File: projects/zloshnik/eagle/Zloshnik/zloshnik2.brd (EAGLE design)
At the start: 132.5 x 50.6 mm, 108 parts, among them IC1 TL5626D, IC2 78L05F, IC6 DS3234, IC7 MEGA8-AI, Q2 IRF630N, Q4 IRF630N, SW1 BUTTON-IT_1181

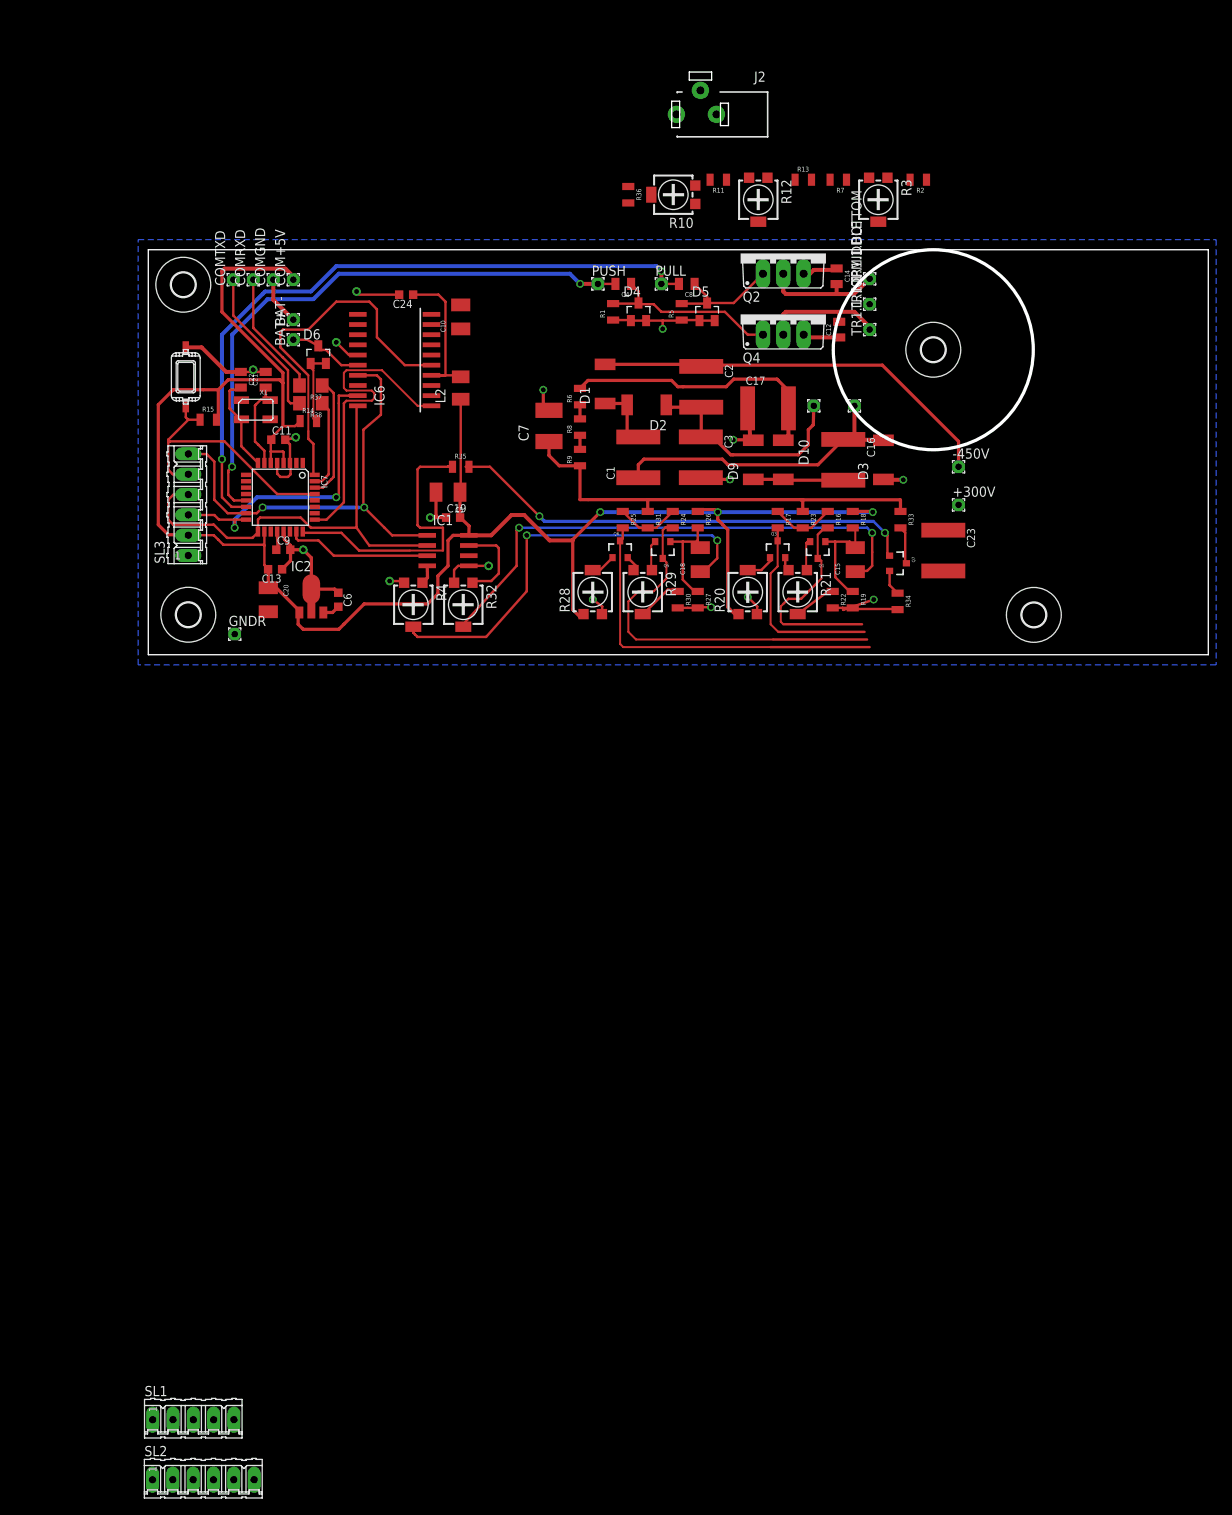
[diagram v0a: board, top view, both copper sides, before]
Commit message: +3v3 and conversion for bluetooth, more sparse layout in hv area
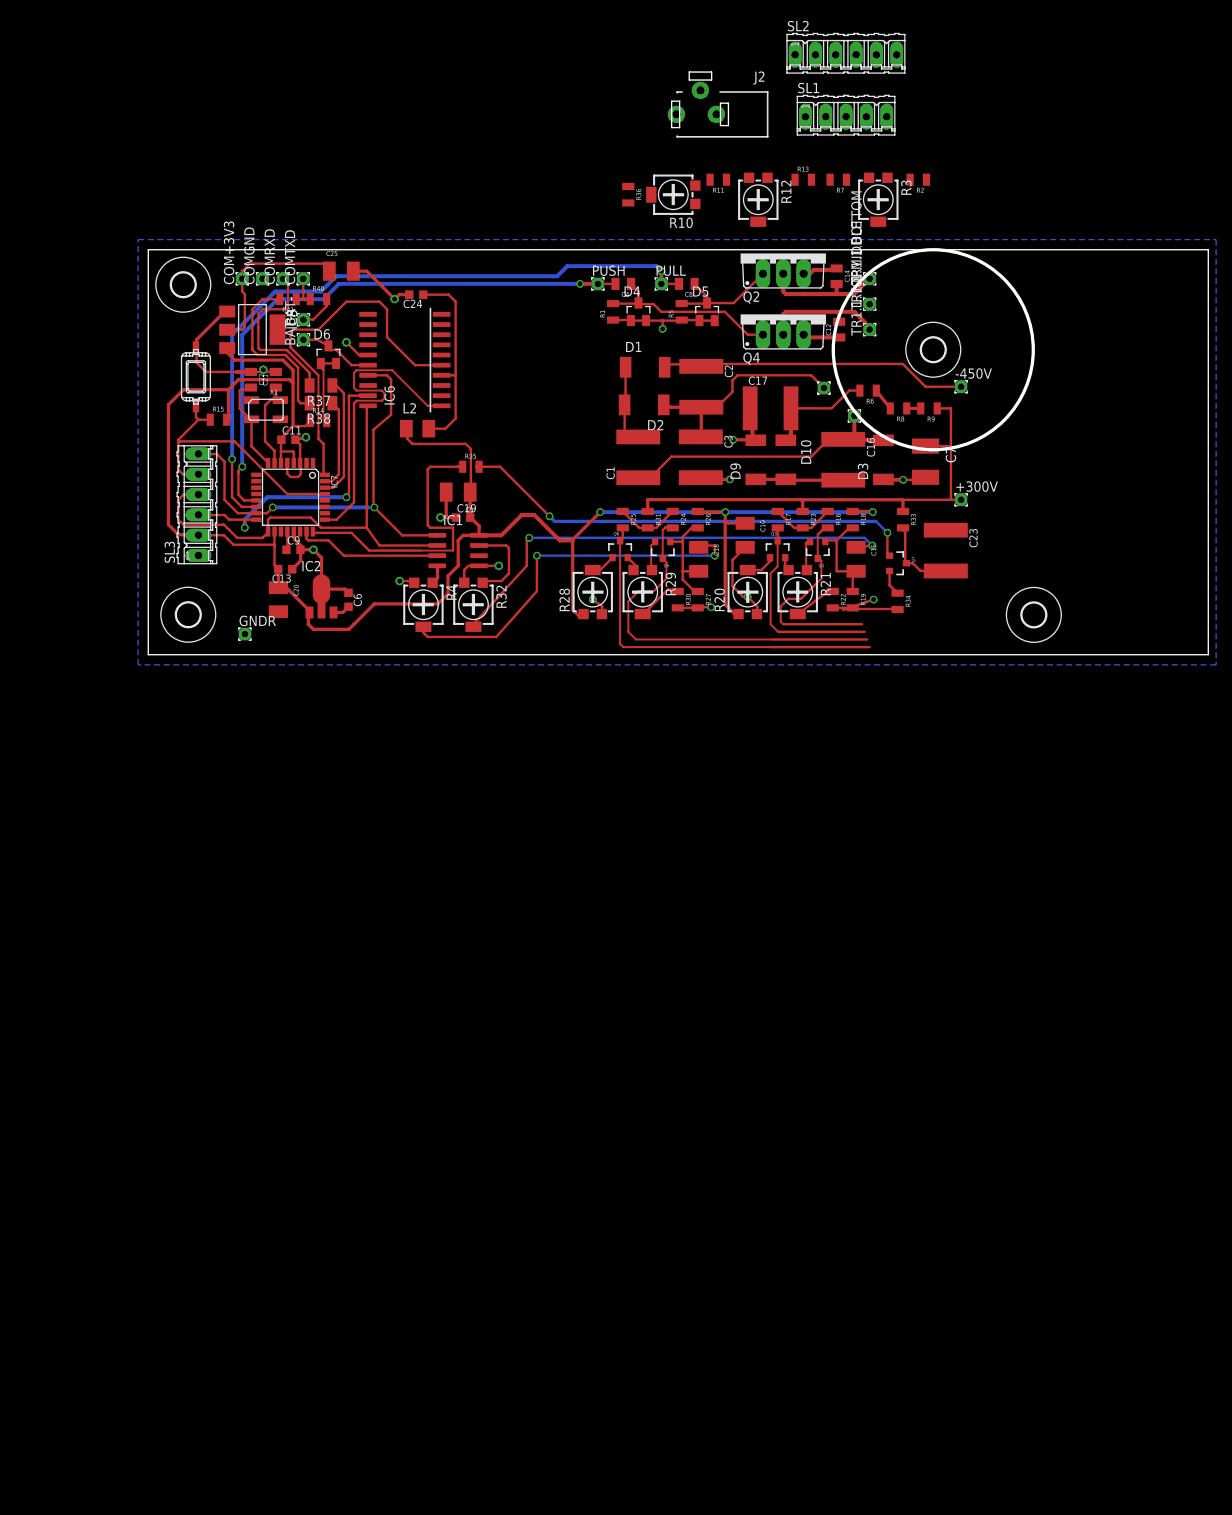
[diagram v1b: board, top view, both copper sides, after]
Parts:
- removed COM+5V: (no value), wirepad:1,6/0,8
- added C25: 10uF, rcl:SMC_B
- added COM+3V3: (no value), wirepad:1,6/0,8
- added IC3: REG1117, burr-brown:SOT223
- added R40: 2k2, rcl:R0805-SVO
- added R41: 1K1, rcl:R0805-SVO
- R37: value 0K -> 0; device rcl:R1206 -> 0-rcl:R1206
- R38: value 0K -> 470; device rcl:R1206 -> 0-rcl:R1206
- moved SL2 195.4 mm to (87.2, 75.0)
- moved SL1 182.2 mm to (87.2, 67.3)
- moved C7 47.3 mm to (97.2, 24.1), turned to 270 degrees
- moved C10 44.8 mm to (74.6, 14.9), turned to 270 degrees
- moved R9 44.1 mm to (97.6, 30.8), turned to 180 degrees
- moved R8 39.9 mm to (93.8, 30.8), turned to 180 degrees
- moved R6 36.0 mm to (90.0, 33.0), turned to 180 degrees
- moved -450V 10.0 mm to (101.6, 33.5)
- moved COMTXD 8.74 mm to (19.4, 47.0)
- moved L2 7.41 mm to (33.7, 28.3), turned to 0 degrees
- moved D1 5.42 mm to (62.1, 35.9), turned to 0 degrees
- moved COMRXD 3.70 mm to (16.8, 47.0)
- moved TR1.2.BOTTOM 2.56 mm to (84.5, 33.3)
- moved COMGND 1.34 mm to (14.3, 47.0)
- moved IC6 1.27 mm to (32.1, 36.8)
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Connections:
- new net +3V3: C25.+, COM+3V3.1, IC3.2
- new net N$3: COMTXD.1, R40.1, R41.1
- net +5V: now also IC3.3; no longer COM+5V.1
- net GND: now also C25.-, IC3.1, R40.2
- net TXD: now also R41.2; no longer COMTXD.1
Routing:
- net +3V3: track 0.00 -> 21.3 mm
- net HV+300UNF: track 34.7 -> 13.8 mm
- net GND: track 133.8 -> 151.7 mm, vias 17 -> 16
- net -450V: track 52.4 -> 40.0 mm
- net +5V: track 240.6 -> 230.5 mm
- net XDAC: track 66.0 -> 59.1 mm
- net YDAC: track 54.2 -> 47.8 mm
- net RXD: track 15.6 -> 21.6 mm
- net RTCVCC: track 19.1 -> 24.6 mm
- net N$34: track 4.77 -> 9.91 mm
- net +300V: track 55.2 -> 60.4 mm
- net N$3: track 0.00 -> 4.37 mm
- net AC_A: track 38.6 -> 35.9 mm
- net TXD: track 19.5 -> 22.0 mm
- net PUSH: track 74.3 -> 72.0 mm
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
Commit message: lots of fixes
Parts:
- removed BAT+, BAT-: (no value), wirepad:1,6/0,8
- removed R41: 1K1, rcl:R0805-SVO
- added CAP+, CAP-: (no value), wirepad:2,54/0,8
- added HEA1, HEA2: (no value), wirepad:1,6/0,8
- C23: value 0,01 1kV -> 0,1 1kV
- R34: value 100K -> 75-100K
- R37: device 0-rcl:R1206 -> rcl:R0805-SVO
- R38: value 470 -> 1K; device 0-rcl:R1206 -> rcl:R0805-SVO
- moved SL2 19.1 mm to (72.4, 62.9)
- moved C24 18.1 mm to (37.6, 27.4), turned to 0 degrees
- moved D6 17.7 mm to (32.0, 22.6)
- moved J2 16.9 mm to (52.5, 70.9), turned to 180 degrees
- moved R36 16.7 mm to (70.8, 70.2)
- moved R3 15.6 mm to (89.9, 72.4)
- moved R11 15.6 mm to (70.9, 74.9)
- moved R12 15.5 mm to (76.2, 72.4)
- moved R10 14.8 mm to (66.0, 72.3), turned to 180 degrees
- moved R14 14.6 mm to (32.1, 19.4), turned to 180 degrees
- moved R13 14.2 mm to (81.6, 73.6), turned to 90 degrees
- moved R7 14.2 mm to (85.1, 73.5), turned to 270 degrees
- moved R2 13.1 mm to (94.6, 72.3), turned to 90 degrees
- moved GNDR 6.99 mm to (11.8, 9.56)
- moved SL1 4.55 mm to (88.9, 63.0), turned to 180 degrees
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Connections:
- net N$36 renamed ZDACN$36
- removed net N$15: R10.3, R11.2
- removed net N$3: COMTXD.1, R40.1, R41.1
- new net N$12: R10.1, R11.2
- net -450V: now also R10.3; no longer R10.1
- net GND: now also CAP-.1; no longer BAT-.1
- net HEATERA: now also HEA1.1
- net HEATERB: now also HEA2.1
- net N$5: now also CAP+.1; no longer BAT+.1
- net TXD: now also COMTXD.1, R40.1; no longer R41.2
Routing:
- net N$5: track 9.46 -> 42.9 mm, vias 0 -> 1
- net +5V: track 230.5 -> 243.7 mm
- net RTCVCC: track 24.6 -> 12.3 mm
- net GND: track 151.7 -> 160.6 mm, vias 16 -> 19
- net RXD: track 21.6 -> 14.8 mm
- net RTCINT: track 45.5 -> 39.1 mm
- net N$10: track 9.45 -> 4.04 mm
- net TXD: track 22.0 -> 27.2 mm
- net N$3: track 4.37 -> 0.00 mm
- net ZDAC: track 37.3 -> 36.0 mm
- net +300V: track 60.4 -> 59.4 mm
- net RTCSEL#: track 40.5 -> 41.4 mm
- net DACSS#: track 18.1 -> 18.7 mm
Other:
- board text added: "2012"

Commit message: stuff
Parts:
- added R39: TRIMPOTSMD, SparkFun:TRIMPOT-3MM
- added R41: TRIMPOT3MM-2, SparkFun:TRIMPOT-3MM-2
- added R42: TRIMPOT-2, SparkFun:TRIMPOT_TC33
- added R47: (no value), 0-rcl:RTRIMTS63Z
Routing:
- net GND: track 160.6 -> 158.6 mm

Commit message: just updated the board
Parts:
- removed R41: TRIMPOT3MM-2, SparkFun:TRIMPOT-3MM-2
- removed R42: TRIMPOT-2, SparkFun:TRIMPOT_TC33
- R39: value TRIMPOTSMD -> (none); device SparkFun:TRIMPOT-3MM -> 0-rcl:RTRIM3314J
- moved R39 46.5 mm to (-11.7, -44.8)
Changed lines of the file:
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@@
 <element name="CAP-" library="wirepad" package="2,54/0,8" value="" x="47.3075" y="36.5125"/>
 <element name="CAP+" library="wirepad" package="2,54/0,8" value="" x="47.3075" y="31.4325"/>
-<element name="R39" library="SparkFun" package="TRIMPOT-3MM" value="TRIMPOTSMD" x="-3.175" y="0.9525"/>
-<element name="R41" library="SparkFun" package="TRIMPOT-3MM-2" value="TRIMPOT3MM-2" x="-6.985" y="1.27"/>
-<element name="R42" library="SparkFun" package="TRIMPOT_TC33" value="TRIMPOT-2" x="-7.3025" y="-3.81"/>
 <element name="R47" library="0-rcl" package="RTRIMTS63Z" value="" x="-10.795" y="-35.56"/>
+<element name="R39" library="0-rcl" package="RTRIM3314J" value="" x="-11.7475" y="-44.7675"/>
 </elements>
 <signals>

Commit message: just updated los values on the schematic
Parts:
- removed R39: (no value), 0-rcl:RTRIM3314J
- removed R47: (no value), 0-rcl:RTRIMTS63Z
- R22, R30: value 2M2 -> 33K
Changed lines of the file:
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@@
 <element name="R20" library="0-rcl" package="RTRIM4G/J" value="10K" x="74.93" y="7.8275"/>
 <element name="R21" library="0-rcl" package="RTRIM4G/J" value="500K" x="81.18" y="7.8275" rot="R180"/>
-<element name="R22" library="rcl" package="R0805-SVO" value="2M2" x="85.555" y="6.885" rot="R270"/>
+<element name="R22" library="rcl" package="R0805-SVO" value="33K" x="85.555" y="6.885" rot="R270"/>
 <element name="R23" library="rcl" package="R0805-SVO" value="0" x="81.805" y="16.885" rot="R270"/>
 <element name="R24" library="rcl" package="R0805-SVO" value="2M2" x="65.555" y="16.885" rot="R270"/>
@@
 <element name="R28" library="0-rcl" package="RTRIM4G/J" value="10K" x="55.555" y="7.8275"/>
 <element name="R29" library="0-rcl" package="RTRIM4G/J" value="500K" x="61.805" y="7.8275" rot="R180"/>
-<element name="R30" library="rcl" package="R0805-SVO" value="2M2" x="66.18" y="6.885" rot="R270"/>
+<element name="R30" library="rcl" package="R0805-SVO" value="33K" x="66.18" y="6.885" rot="R270"/>
 <element name="R31" library="rcl" package="R0805-SVO" value="0" x="62.43" y="16.885" rot="R270"/>
 <element name="IC1" library="0-tlv5626" package="SO08" value="TL5626D" x="38.735" y="13.0175" rot="R270"/>
@@
 <element name="CAP-" library="wirepad" package="2,54/0,8" value="" x="47.3075" y="36.5125"/>
 <element name="CAP+" library="wirepad" package="2,54/0,8" value="" x="47.3075" y="31.4325"/>
-<element name="R47" library="0-rcl" package="RTRIMTS63Z" value="" x="-10.795" y="-35.56"/>
-<element name="R39" library="0-rcl" package="RTRIM3314J" value="" x="-11.7475" y="-44.7675"/>
 </elements>
 <signals>

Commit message: updates in part values
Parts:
- IC1: value TL5626D -> TLV5626D
- R16, R24: value 2M2 -> 1M
- R17, R25: value 4M7 -> 1M
- R21, R29: value 500K -> 5K
- R22, R30: value 33K -> 10K
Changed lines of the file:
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@@
 <element name="R12" library="0-rcl" package="RTRIM4G/J" value="500K" x="76.2" y="72.39" rot="R180"/>
 <element name="R13" library="rcl" package="R0805-SVO" value="2M" x="81.595" y="73.62" rot="R90"/>
-<element name="R16" library="rcl" package="R0805-SVO" value="2M2" x="84.93" y="16.885" rot="R270"/>
-<element name="R17" library="rcl" package="R0805-SVO" value="4M7" x="78.68" y="16.885" rot="R270"/>
+<element name="R16" library="rcl" package="R0805-SVO" value="1M" x="84.93" y="16.885" rot="R270"/>
+<element name="R17" library="rcl" package="R0805-SVO" value="1M" x="78.68" y="16.885" rot="R270"/>
 <element name="Q1" library="SparkFun" package="SOT23-3" value="" x="83.68" y="13.135" rot="R180"/>
 <element name="Q3" library="SparkFun" package="SOT23-3" value="" x="78.67" y="13.135"/>
@@
 <element name="C15" library="rcl" package="SMC_B" value="10uF" x="88.475" y="11.9275" rot="R270"/>
 <element name="R20" library="0-rcl" package="RTRIM4G/J" value="10K" x="74.93" y="7.8275"/>
-<element name="R21" library="0-rcl" package="RTRIM4G/J" value="500K" x="81.18" y="7.8275" rot="R180"/>
-<element name="R22" library="rcl" package="R0805-SVO" value="33K" x="85.555" y="6.885" rot="R270"/>
+<element name="R21" library="0-rcl" package="RTRIM4G/J" value="5K" x="81.18" y="7.8275" rot="R180"/>
+<element name="R22" library="rcl" package="R0805-SVO" value="10K" x="85.555" y="6.885" rot="R270"/>
 <element name="R23" library="rcl" package="R0805-SVO" value="0" x="81.805" y="16.885" rot="R270"/>
-<element name="R24" library="rcl" package="R0805-SVO" value="2M2" x="65.555" y="16.885" rot="R270"/>
-<element name="R25" library="rcl" package="R0805-SVO" value="4M7" x="59.305" y="16.885" rot="R270"/>
+<element name="R24" library="rcl" package="R0805-SVO" value="1M" x="65.555" y="16.885" rot="R270"/>
+<element name="R25" library="rcl" package="R0805-SVO" value="1M" x="59.305" y="16.885" rot="R270"/>
 <element name="Q5" library="SparkFun" package="SOT23-3" value="" x="64.305" y="13.135" rot="R180"/>
 <element name="Q6" library="SparkFun" package="SOT23-3" value="" x="58.9775" y="13.135"/>
@@
 <element name="C18" library="rcl" package="SMC_B" value="10uF" x="68.7975" y="11.9275" rot="R270"/>
 <element name="R28" library="0-rcl" package="RTRIM4G/J" value="10K" x="55.555" y="7.8275"/>
-<element name="R29" library="0-rcl" package="RTRIM4G/J" value="500K" x="61.805" y="7.8275" rot="R180"/>
-<element name="R30" library="rcl" package="R0805-SVO" value="33K" x="66.18" y="6.885" rot="R270"/>
+<element name="R29" library="0-rcl" package="RTRIM4G/J" value="5K" x="61.805" y="7.8275" rot="R180"/>
+<element name="R30" library="rcl" package="R0805-SVO" value="10K" x="66.18" y="6.885" rot="R270"/>
 <element name="R31" library="rcl" package="R0805-SVO" value="0" x="62.43" y="16.885" rot="R270"/>
-<element name="IC1" library="0-tlv5626" package="SO08" value="TL5626D" x="38.735" y="13.0175" rot="R270"/>
+<element name="IC1" library="0-tlv5626" package="SO08" value="TLV5626D" x="38.735" y="13.0175" rot="R270"/>
 <element name="C19" library="rcl" package="C0603K" value="100nF" x="39.37" y="17.145"/>
 <element name="R4" library="0-rcl" package="RTRIM4G/J" value="10K" x="34.395" y="6.25" rot="R180"/>

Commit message: latest fixes for 3loshnik schematics
morsekeyer
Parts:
- R33: value 2M2 -> 470K
- R34: value 75-100K -> 10K
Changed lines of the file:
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@@
 <element name="C22" library="rcl" package="C0805S" value="18pF" x="12.8275" y="34.375" rot="R270"/>
 <element name="Q7" library="SparkFun" package="SOT23-3" value="" x="93.6625" y="11.43" rot="R270"/>
-<element name="R33" library="rcl" package="R0805-SVO" value="2M2" x="94.34" y="16.885" rot="R270"/>
-<element name="R34" library="rcl" package="R0805-SVO" value="75-100K" x="93.6625" y="6.6675" rot="R270"/>
+<element name="R33" library="rcl" package="R0805-SVO" value="470K" x="94.34" y="16.885" rot="R270"/>
+<element name="R34" library="rcl" package="R0805-SVO" value="10K" x="93.6625" y="6.6675" rot="R270"/>
 <element name="R35" library="rcl" package="R0805-SVO" value="1K" x="40.3225" y="23.495"/>
 <element name="C23" library="0-rcl" package="C2220K" value="0,1 1kV" x="100.0125" y="13.0175" rot="R270"/>
